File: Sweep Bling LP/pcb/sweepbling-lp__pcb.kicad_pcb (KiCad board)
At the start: 2 copper layers, 216.9 x 86.9 mm, 51 parts, among them J1 AudioJack4dpb, J2 AudioJack4dpb, SW10 SW_Push, SW11 SW_Push, SW11_r1 SW_Push, SW12 SW_Push, SW12_r1 SW_Push, SW13_r1 SW_Push, SW14 SW_Push, SW15 SW_Push, SW15_r1 SW_Push, SW16 SW_Push, SW16_r1 SW_Push, SW17 SW_Push, SW17_r1 SW_Push, SW18 SW_Push, SW18_r1 SW_Push, SW2 SW_Push, SW20 SW_Push, SW20_r1 SW_Push, SW21 SW_Push, SW21_r1 SW_Push, SW2_r1 SW_Push, SW3 SW_Push, SW3_r1 SW_Push, SW4 SW_Push, SW4_r1 SW_Push, SW5 SW_Push, SW5_r1 SW_Push, SW6 SW_Push, SW6_r1 SW_Push, SW7_r1 SW_Push, SW8 SW_Push, SW8_r1 SW_Push, SW9 SW_Push, SW9_r1 SW_Push, U1 ProMicro-kbd, U2 ProMicro-kbd

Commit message: Fix schematic
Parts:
- SW_POWER1, SW_POWERR1: renamed from POWER SW
- TRRS1: renamed from J2; value AudioJack4dpb -> AudioJack4; footprint Kailh:TRRS-PJ-320A -> * duckyb-collection:TRRS-PJ-320A
- TRRS2: renamed from J1; value AudioJack4dpb -> AudioJack4; footprint Kailh:TRRS-PJ-320A -> * duckyb-collection:TRRS-PJ-320A
- renumbered B+ to Bat+1, B+ to Bat+r1, B- to BatGND1, B- to BatGNDr1, SW2 to SW1, SW12 to SW10, SW12_r1 to SW10_r1, SW14 to SW11, SW13_r1 to SW11_r1, SW15 to SW12, SW18_r1 to SW12_r1, SW16 to SW13, SW15_r1 to SW13_r1, SW17 to SW14, SW16_r1 to SW14_r1, SW18 to SW15, SW17_r1 to SW15_r1, SW21 to SW16, SW21_r1 to SW16_r1, SW20 to SW17, SW20_r1 to SW17_r1, SW2_r1 to SW1_r1, SW3 to SW2, SW3_r1 to SW2_r1, SW4 to SW3, SW4_r1 to SW3_r1, SW5 to SW4, SW5_r1 to SW4_r1, SW6 to SW5, SW6_r1 to SW5_r1, SW8 to SW6, SW7_r1 to SW6_r1, SW9 to SW7, SW8_r1 to SW7_r1, SW10 to SW8, SW9_r1 to SW8_r1, SW11 to SW9, SW11_r1 to SW9_r1, G*** to SweepLogo, REF_PUCK_L to e, mouse-bite-2mm-slot to mouse-bite-2mm-slot1, mouse-bite-2mm-slot to mouse-bite-2mm-slot2
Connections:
- Bat+1 pad 1: BT+_r -> BT+
- Bat+r1 pad 1: BT+ -> BT+_r
- BatGNDr1 pad 1: gnd -> gnd_r
- RSW2 pad 1: gnd -> gnd_r
- SW10_r1 pad 2: gnd -> gnd_r
- SW11_r1 pad 2: gnd -> gnd_r
- SW12_r1 pad 2: gnd -> gnd_r
- SW13_r1 pad 2: gnd -> gnd_r
- SW14_r1 pad 2: gnd -> gnd_r
- SW15_r1 pad 2: gnd -> gnd_r
- SW16_r1 pad 2: gnd -> gnd_r
- SW17_r1 pad 2: gnd -> gnd_r
- SW1_r1 pad 2: gnd -> gnd_r
- SW2_r1 pad 2: gnd -> gnd_r
- SW3_r1 pad 2: gnd -> gnd_r
- SW4_r1 pad 2: gnd -> gnd_r
- SW5_r1 pad 2: gnd -> gnd_r
- SW6_r1 pad 2: gnd -> gnd_r
- SW7_r1 pad 2: gnd -> gnd_r
- SW8_r1 pad 2: gnd -> gnd_r
- SW9_r1 pad 2: gnd -> gnd_r
- SW_POWER1 pad 1: Net-(SW_POWERR1-Pad1) -> unconnected-(SW_POWER1-Pad1)
- SW_POWER1 pad 2: BT+_r -> BT+
- SW_POWERR1 pad 1: Net-(SW_POWER1-Pad1) -> unconnected-(SW_POWERR1-Pad1)
- SW_POWERR1 pad 2: BT+ -> BT+_r
- SW_POWERR1 pad 3: raw -> raw_r
- TRRS2 pad R2: vcc -> vcc_r
- TRRS2 pad S: gnd -> gnd_r
- TRRS2 pad T: gnd -> gnd_r
- U2 pad 21: vcc -> vcc_r
- U2 pad 23: gnd -> gnd_r
- U2 pad 24: raw -> raw_r
- U2 pad 3: gnd -> gnd_r
- U2 pad 4: gnd -> gnd_r
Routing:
- net vcc_r: track 0.00 -> 26.0 mm, vias 0 -> 1
- net vcc: track 58.1 -> 32.1 mm, vias 2 -> 1
- net raw_r: track 0.00 -> 12.3 mm
- net raw: track 23.8 -> 11.5 mm
- net BT+_r: track 6.47 -> 10.3 mm
- net BT+: track 10.3 -> 6.47 mm
- net gnd_r: vias 0 -> 3
- net gnd: vias 4 -> 3
- added copper zone on B.Cu, net gnd_r
- added copper zone on F.Cu, net gnd_r
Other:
- board text added: "B+"
- board text added: "B-"
- board text added: "GND"
- board text added: "POWER"

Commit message: Update bling-lp pcb
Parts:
- added REF**: MountingHole_3.2mm_M3, MountingHole:MountingHole_3.2mm_M3, F.Cu at (203.9, 28.2)
- added REF**: MountingHole_3.2mm_M3, MountingHole:MountingHole_3.2mm_M3, F.Cu at (56.6, 28.2)
- added REF**: MountingHole_3.2mm_M3, MountingHole:MountingHole_3.2mm_M3, F.Cu at (110.1, 82.4)
- added REF**: MountingHole_3.2mm_M3, MountingHole:MountingHole_3.2mm_M3, F.Cu at (29.0, 91.6)
- added REF**: MountingHole_3.2mm_M3, MountingHole:MountingHole_3.2mm_M3, F.Cu at (231.6, 91.6)
- added REF**: MountingHole_3.2mm_M3, MountingHole:MountingHole_3.2mm_M3, F.Cu at (150.5, 82.4)
- added REF**: MountingHole_3.2mm_M3, MountingHole:MountingHole_3.2mm_M3, F.Cu at (113.7, 38.4)
- added REF**: MountingHole_3.2mm_M3, MountingHole:MountingHole_3.2mm_M3, F.Cu at (146.9, 38.4)
- REF_PUCK_R, e: footprint kbd:Tenting_Puck2 -> * duckyb-collection:Tenting_Puck2_no_pads
- SW1, SW10, SW10_r1, SW11, SW11_r1, SW12, SW12_r1, SW13, SW13_r1, SW14, SW14_r1, SW15, SW15_r1, SW16, SW16_r1, SW17, SW17_r1, SW1_r1, SW2, SW2_r1, SW3, SW3_r1, SW4, SW4_r1, SW5, SW5_r1, SW6, SW6_r1, SW7, SW7_r1, SW8, SW8_r1, SW9, SW9_r1: footprint * duckyb-collection:SW_Hotswap_Kailh_Choc_V1_no_bounds -> * duckyb-collection:SW_Hotswap_Kailh_Choc_V1_tweaked
- moved RSW1 0.51 mm to (222.4, 85.7)
- moved RSW2 0.13 mm to (38.0, 85.7)
- turned SW13_r1 to 180 degrees
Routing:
- net Switch13_r: track 47.3 -> 60.1 mm
- net Switch12_r: track 86.7 -> 80.2 mm
- net Switch11_r: track 107.8 -> 101.4 mm
- net Switch16: track 44.2 -> 40.6 mm
- net Switch17: track 30.4 -> 33.8 mm
- net reset: track 30.4 -> 29.9 mm
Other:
- board text added: "v1.0"
- board text removed: "GND"
- board text removed: "v0.1 α"

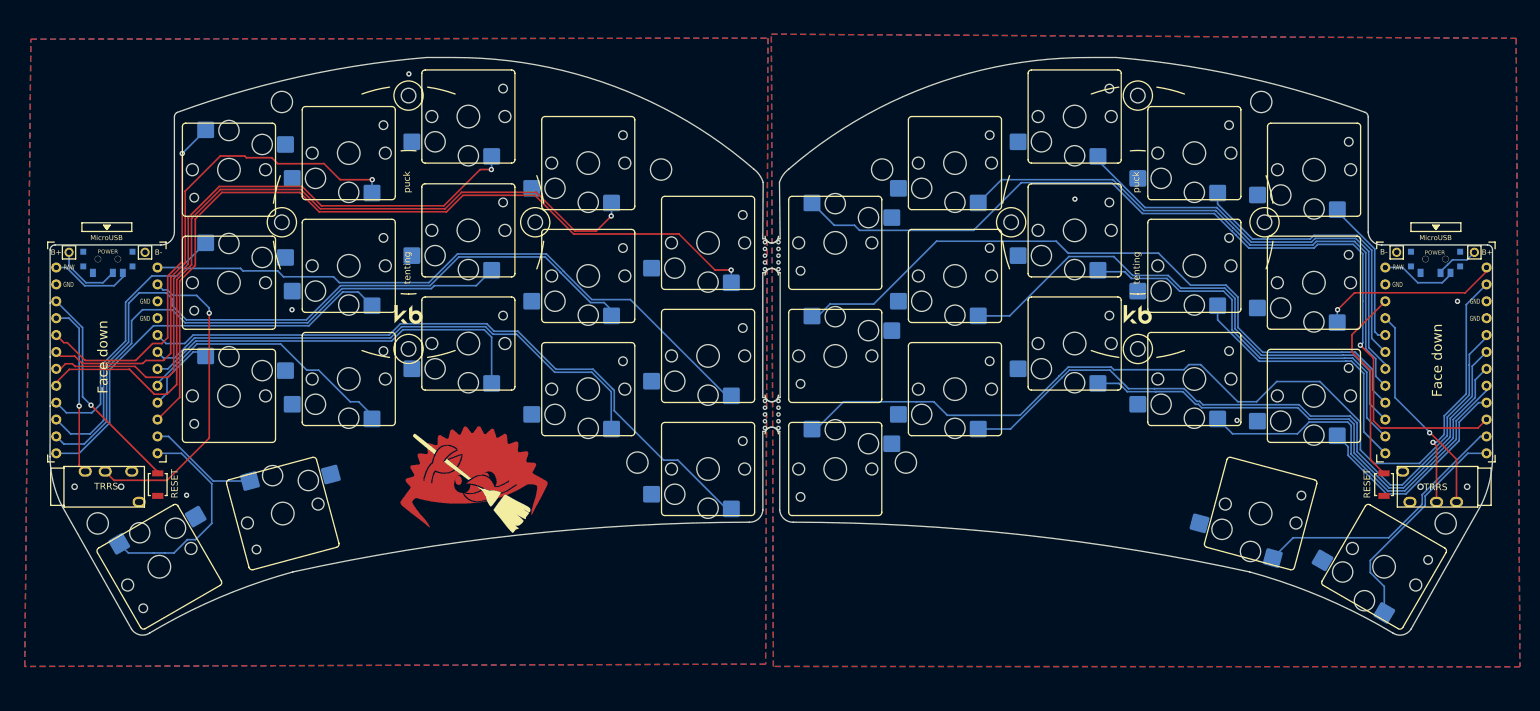
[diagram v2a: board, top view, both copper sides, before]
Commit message: Update Bling LP spacer hole diameter & gerber
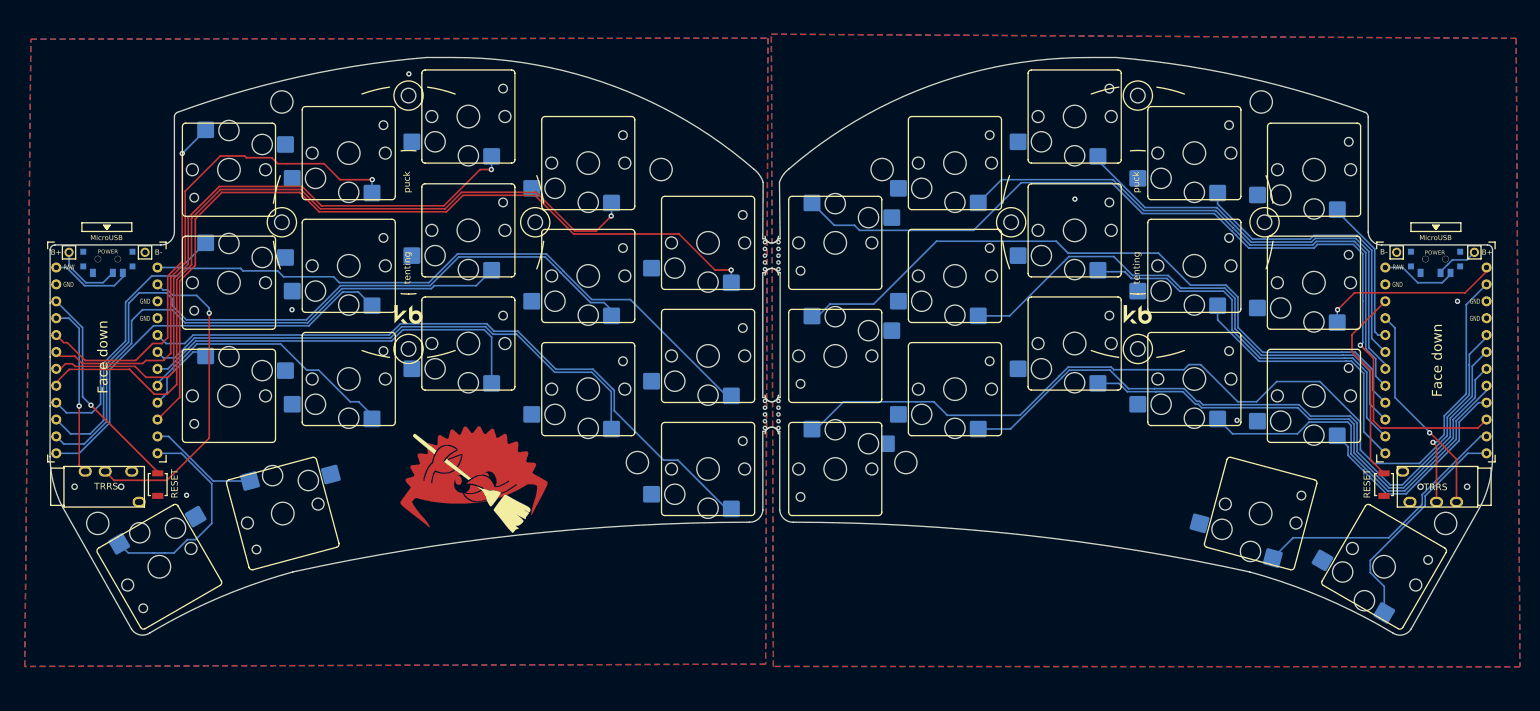
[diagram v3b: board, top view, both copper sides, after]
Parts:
- REF** (x8): value MountingHole_3.2mm_M3 -> MountingHole_3.35mm; footprint MountingHole:MountingHole_3.2mm_M3 -> duckyb-footprints:MountingHole_3.35mm
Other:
- board text added: "v1.1"
- board text removed: "v1.0"
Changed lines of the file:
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@@
     (fp_line (start 7 6.5) (end 7 -6.5) (layer "F.SilkS") (width 0.12))
     (fp_line (start -6.5 7) (end 6.5 7) (layer "F.SilkS") (width 0.12))
-    (fp_arc (start -7 -6.5) (mid -6.853554 -6.853553) (end -6.5 -7) (layer "F.SilkS") (width 0.12))
+    (fp_arc (start -7 -6.5) (mid -6.853553 -6.853553) (end -6.5 -7) (layer "F.SilkS") (width 0.12))
     (fp_arc (start 7 6.5) (mid 6.853553 6.853553) (end 6.5 7) (layer "F.SilkS") (width 0.12))
     (fp_arc (start 6.5 -7) (mid 6.853553 -6.853553) (end 7 -6.5) (layer "F.SilkS") (width 0.12))
-    (fp_arc (start -6.5 7) (mid -6.853553 6.853554) (end -7 6.5) (layer "F.SilkS") (width 0.12))
+    (fp_arc (start -6.5 7) (mid -6.853553 6.853553) (end -7 6.5) (layer "F.SilkS") (width 0.12))
     (fp_rect (start -7 -7) (end 7 7) (layer "Dwgs.User") (width 0.12) (fill none))
     (fp_line (start 7.25 7.25) (end 7.25 -7.25) (layer "Eco1.User") (width 0.1))
@@
     (pad "1" smd roundrect (at -3.5 -6) (size 2.55 2.5) (layers "B.Cu" "B.Paste" "B.Mask") (roundrect_rratio 0.1)
       (net 15 "Switch11") (pinfunction "1") (pintype "passive"))
-    (pad "2" smd roundrect (at 8.5 -3.8) (size 2.55 2.5) (layers "B.Cu" "B.Paste" "B.Mask") (roundrect_rratio 0.1)
+    (pad "2" smd roundrect (at 7.95 -3.8) (size 2 2.5) (layers "B.Cu" "B.Paste" "B.Mask") (roundrect_rratio 0.1)
       (net 1 "gnd") (pinfunction "2") (pintype "passive"))
     (model "${KICAD6_3RD_PARTY}/3dmodels/com_github_perigoso_keyswitch-kicad-library/3d-library.3dshapes/SW_Hotswap_Kailh_Choc_v1.stp"
@@
     (fp_line (start -6.5 7) (end 6.5 7) (layer "F.SilkS") (width 0.12))
     (fp_line (start 6.5 -7) (end -6.5 -7) (layer "F.SilkS") (width 0.12))
-    (fp_arc (start -7 -6.5) (mid -6.853554 -6.853553) (end -6.5 -7) (layer "F.SilkS") (width 0.12))
+    (fp_arc (start -7 -6.5) (mid -6.853553 -6.853553) (end -6.5 -7) (layer "F.SilkS") (width 0.12))
     (fp_arc (start 6.5 -7) (mid 6.853553 -6.853553) (end 7 -6.5) (layer "F.SilkS") (width 0.12))
-    (fp_arc (start -6.5 7) (mid -6.853553 6.853554) (end -7 6.5) (layer "F.SilkS") (width 0.12))
+    (fp_arc (start -6.5 7) (mid -6.853553 6.853553) (end -7 6.5) (layer "F.SilkS") (width 0.12))
     (fp_arc (start 7 6.5) (mid 6.853553 6.853553) (end 6.5 7) (layer "F.SilkS") (width 0.12))
     (fp_rect (start -7 -7) (end 7 7) (layer "Dwgs.User") (width 0.12) (fill none))
@@
     )
   )
-  (footprint "MountingHole:MountingHole_3.2mm_M3" (layer "F.Cu")
+  (footprint "duckyb-footprints:MountingHole_3.35mm" (layer "F.Cu")
     (at 203.918 28.194)
     (descr "Mounting Hole 3.2mm, no annular, M3")
@@
       (effects (font (size 1 1) (thickness 0.15)))
     )
-    (fp_text value "MountingHole_3.2mm_M3" (at 0 4.2) (layer "F.Fab")
+    (fp_text value "MountingHole_3.35mm" (at 0 4.2) (layer "F.Fab")
       (effects (font (size 1 1) (thickness 0.15)))
     )
@@
     (fp_circle (center 0 0) (end 3.2 0) (layer "Cmts.User") (width 0.15) (fill none))
     (fp_circle (center 0 0) (end 3.45 0) (layer "F.CrtYd") (width 0.05) (fill none))
-    (pad "" np_thru_hole circle (at 0 0) (size 3.2 3.2) (drill 3.2) (layers *.Cu *.Mask))
+    (pad "" np_thru_hole circle (at 0 0) (size 3.35 3.35) (drill 3.35) (layers F&B.Cu *.Mask))
   )
-  (footprint "MountingHole:MountingHole_3.2mm_M3" (layer "F.Cu")
+  (footprint "duckyb-footprints:MountingHole_3.35mm" (layer "F.Cu")
     (at 56.642 28.194)
     (descr "Mounting Hole 3.2mm, no annular, M3")
@@
       (effects (font (size 1 1) (thickness 0.15)))
     )
-    (fp_text value "MountingHole_3.2mm_M3" (at 0 4.2) (layer "F.Fab")
+    (fp_text value "MountingHole_3.35mm" (at 0 4.2) (layer "F.Fab")
       (effects (font (size 1 1) (thickness 0.15)))
     )
@@
     (fp_circle (center 0 0) (end 3.2 0) (layer "Cmts.User") (width 0.15) (fill none))
     (fp_circle (center 0 0) (end 3.45 0) (layer "F.CrtYd") (width 0.05) (fill none))
-    (pad "" np_thru_hole circle (at 0 0) (size 3.2 3.2) (drill 3.2) (layers *.Cu *.Mask))
+    (pad "" np_thru_hole circle (at 0 0) (size 3.35 3.35) (drill 3.35) (layers F&B.Cu *.Mask))
   )
-  (footprint "MountingHole:MountingHole_3.2mm_M3" (layer "F.Cu")
+  (footprint "duckyb-footprints:MountingHole_3.35mm" (layer "F.Cu")
     (at 110.109 82.41961)
     (descr "Mounting Hole 3.2mm, no annular, M3")
@@
       (effects (font (size 1 1) (thickness 0.15)))
     )
-    (fp_text value "MountingHole_3.2mm_M3" (at 0 4.2) (layer "F.Fab")
+    (fp_text value "MountingHole_3.35mm" (at 0 4.2) (layer "F.Fab")
       (effects (font (size 1 1) (thickness 0.15)))
     )
@@
     (fp_circle (center 0 0) (end 3.2 0) (layer "Cmts.User") (width 0.15) (fill none))
     (fp_circle (center 0 0) (end 3.45 0) (layer "F.CrtYd") (width 0.05) (fill none))
-    (pad "" np_thru_hole circle (at 0 0) (size 3.2 3.2) (drill 3.2) (layers *.Cu *.Mask))
+    (pad "" np_thru_hole circle (at 0 0) (size 3.35 3.35) (drill 3.35) (layers F&B.Cu *.Mask))
   )
-  (footprint "MountingHole:MountingHole_3.2mm_M3" (layer "F.Cu")
+  (footprint "duckyb-footprints:MountingHole_3.35mm" (layer "F.Cu")
     (at 28.956 91.567)
     (descr "Mounting Hole 3.2mm, no annular, M3")
@@
       (effects (font (size 1 1) (thickness 0.15)))
     )
-    (fp_text value "MountingHole_3.2mm_M3" (at 0 4.2) (layer "F.Fab")
+    (fp_text value "MountingHole_3.35mm" (at 0 4.2) (layer "F.Fab")
       (effects (font (size 1 1) (thickness 0.15)))
     )
@@
     (fp_circle (center 0 0) (end 3.2 0) (layer "Cmts.User") (width 0.15) (fill none))
     (fp_circle (center 0 0) (end 3.45 0) (layer "F.CrtYd") (width 0.05) (fill none))
-    (pad "" np_thru_hole circle (at 0 0) (size 3.2 3.2) (drill 3.2) (layers *.Cu *.Mask))
+    (pad "" np_thru_hole circle (at 0 0) (size 3.35 3.35) (drill 3.35) (layers F&B.Cu *.Mask))
   )
-  (footprint "MountingHole:MountingHole_3.2mm_M3" (layer "F.Cu")
+  (footprint "duckyb-footprints:MountingHole_3.35mm" (layer "F.Cu")
     (at 231.648 91.567)
     (descr "Mounting Hole 3.2mm, no annular, M3")
@@
       (effects (font (size 1 1) (thickness 0.15)))
     )
-    (fp_text value "MountingHole_3.2mm_M3" (at 0 4.2) (layer "F.Fab")
+    (fp_text value "MountingHole_3.35mm" (at 0 4.2) (layer "F.Fab")
       (effects (font (size 1 1) (thickness 0.15)))
     )
@@
     (fp_circle (center 0 0) (end 3.2 0) (layer "Cmts.User") (width 0.15) (fill none))
     (fp_circle (center 0 0) (end 3.45 0) (layer "F.CrtYd") (width 0.05) (fill none))
-    (pad "" np_thru_hole circle (at 0 0) (size 3.2 3.2) (drill 3.2) (layers *.Cu *.Mask))
+    (pad "" np_thru_hole circle (at 0 0) (size 3.35 3.35) (drill 3.35) (layers F&B.Cu *.Mask))
   )
-  (footprint "MountingHole:MountingHole_3.2mm_M3" (layer "F.Cu")
+  (footprint "duckyb-footprints:MountingHole_3.35mm" (layer "F.Cu")
     (at 150.479 82.41961)
     (descr "Mounting Hole 3.2mm, no annular, M3")
@@
       (effects (font (size 1 1) (thickness 0.15)))
     )
-    (fp_text value "MountingHole_3.2mm_M3" (at 0 4.2) (layer "F.Fab")
+    (fp_text value "MountingHole_3.35mm" (at 0 4.2) (layer "F.Fab")
       (effects (font (size 1 1) (thickness 0.15)))
     )
@@
     (fp_circle (center 0 0) (end 3.2 0) (layer "Cmts.User") (width 0.15) (fill none))
     (fp_circle (center 0 0) (end 3.45 0) (layer "F.CrtYd") (width 0.05) (fill none))
-    (pad "" np_thru_hole circle (at 0 0) (size 3.2 3.2) (drill 3.2) (layers *.Cu *.Mask))
+    (pad "" np_thru_hole circle (at 0 0) (size 3.35 3.35) (drill 3.35) (layers F&B.Cu *.Mask))
   )
-  (footprint "MountingHole:MountingHole_3.2mm_M3" (layer "F.Cu")
+  (footprint "duckyb-footprints:MountingHole_3.35mm" (layer "F.Cu")
     (at 113.665 38.354)
     (descr "Mounting Hole 3.2mm, no annular, M3")
@@
       (effects (font (size 1 1) (thickness 0.15)))
     )
-    (fp_text value "MountingHole_3.2mm_M3" (at 0 4.2) (layer "F.Fab")
+    (fp_text value "MountingHole_3.35mm" (at 0 4.2) (layer "F.Fab")
       (effects (font (size 1 1) (thickness 0.15)))
     )
@@
     (fp_circle (center 0 0) (end 3.2 0) (layer "Cmts.User") (width 0.15) (fill none))
     (fp_circle (center 0 0) (end 3.45 0) (layer "F.CrtYd") (width 0.05) (fill none))
-    (pad "" np_thru_hole circle (at 0 0) (size 3.2 3.2) (drill 3.2) (layers *.Cu *.Mask))
+    (pad "" np_thru_hole circle (at 0 0) (size 3.35 3.35) (drill 3.35) (layers F&B.Cu *.Mask))
   )
-  (footprint "MountingHole:MountingHole_3.2mm_M3" (layer "F.Cu")
+  (footprint "duckyb-footprints:MountingHole_3.35mm" (layer "F.Cu")
     (at 146.905 38.354)
     (descr "Mounting Hole 3.2mm, no annular, M3")
@@
       (effects (font (size 1 1) (thickness 0.15)))
     )
-    (fp_text value "MountingHole_3.2mm_M3" (at 0 4.2) (layer "F.Fab")
+    (fp_text value "MountingHole_3.35mm" (at 0 4.2) (layer "F.Fab")
       (effects (font (size 1 1) (thickness 0.15)))
     )
@@
     (fp_circle (center 0 0) (end 3.2 0) (layer "Cmts.User") (width 0.15) (fill none))
     (fp_circle (center 0 0) (end 3.45 0) (layer "F.CrtYd") (width 0.05) (fill none))
-    (pad "" np_thru_hole circle (at 0 0) (size 3.2 3.2) (drill 3.2) (layers *.Cu *.Mask))
+    (pad "" np_thru_hole circle (at 0 0) (size 3.35 3.35) (drill 3.35) (layers F&B.Cu *.Mask))
   )
   (footprint "Kailh:SPDT_C128955" (layer "B.Cu")
@@
   (gr_line (start 131.5085 77.724) (end 131.2545 77.724) (layer "Edge.Cuts") (width 0.05))
   (gr_arc (start 129.349501 53.848) (mid 130.302 53.203127) (end 131.254499 53.848001) (layer "Edge.Cuts") (width 0.05))
-  (gr_text "v1.0" (at 140.97 39.116) (layer "B.SilkS")
+  (gr_text "v1.1" (at 140.97 39.116) (layer "B.SilkS")
     (effects (font (size 1.5 1.5) (thickness 0.3)) (justify mirror))
   )
